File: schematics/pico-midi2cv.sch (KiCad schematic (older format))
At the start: 30 parts, among them J1 Jack-DC, U1 LM7805_TO220, U2 LM358, U3 MCP4822, U4 6N138

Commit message: Updated schematics
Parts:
- removed J_CV1, J_GATE1: CV Out, symbol Connector:AudioJack2
- removed J_SWD_IO1: UART Programming, symbol Connector:Conn_01x02_Male
- added H1, H2, H3: MountingHole, MountingHole:MountingHole_3mm, symbol Mechanical:MountingHole
- added J_CV1: CV Out, Zimo_Manual_PCB:NSL25_01x02_Vertical, symbol Connector:Conn_01x02_Male
- added J_GATE1: Gate Out, Zimo_Manual_PCB:NSL25_01x02_Vertical, symbol Connector:Conn_01x02_Male
- added J_SWD_IO1: UART Programming, Zimo_Manual_PCB:PinOut_01x04, symbol Connector:Conn_01x04_Male
- C1: footprint (none) -> Zimo_Manual_PCB:CP_Radial_D5.0mm_P2.50mm
- C2, C3, C4, C5, C6: footprint (none) -> Zimo_Manual_PCB:C_Disc_D5.0mm_W2.5mm_P2.50mm
- D1: footprint (none) -> Zimo_Manual_PCB:D_Axial
- D_GATE_LED1: footprint (none) -> Zimo_Manual_PCB:NSL25_01x02_Vertical
- J1: value Jack-DC -> Jack-DC (12-32V); footprint (none) -> Zimo_Manual_PCB:NSL25_01x02_Vertical
- J_MIDI_IN1: footprint (none) -> Zimo_Manual_PCB:PinOut_01x05
- Q_GATE_LED1: footprint Package_TO_SOT_THT:TO-92_Inline -> Zimo_Manual_PCB:TO-92_Inline_Wide
- R1, R11, R2, R3, R4, R5, R6, R7, R8, R9: footprint (none) -> Zimo_Manual_PCB:R_Axial_Vertical
- R10: value 220 -> 470; footprint (none) -> Zimo_Manual_PCB:R_Axial_Vertical
- U2, U3, U4: footprint (none) -> Zimo_Manual_PCB:DIP-8_W7.62mm
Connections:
- net +5V: now also J_SWD_IO1.3 (Pin_3)
- net GND: now also J_CV1.2 (Pin_2), J_GATE1.2 (Pin_2), J_SWD_IO1.4 (Pin_4)
- net UART_RX: now also J_SWD_IO1.2 (Pin_2)
- net UART_TX: now also J_SWD_IO1.1 (Pin_1)
- net at R3.1: now also J_CV1.1 (Pin_1)
- net at R8.1: now also J_GATE1.1 (Pin_1)
- no-connect marks 7 -> 31

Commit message: Updated schematics
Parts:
- added D2: 1N4001, Zimo_Manual_PCB:D_Axial, symbol Device:D
- R5: value 22k -> 100k
- R6: value 33k -> 51k
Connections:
- net +12V: now also D2.2 (A); no longer C1.1, C2.1, U1.1 (VI)
- net at C5.1, R3.2, U2.1: no longer R2.1
- net at J_CV1.1 (Pin_1), R3.1: now also R2.1
- new net: C1.1, C2.1, D2.1 (K), U1.1 (VI)
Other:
- note added: "Calibration\n————————\nThe max output of the DAC is 4095mV. At this\npoint the CV output should be 10000mV (10V)\nto cover the 10 octave range. This is an ampli-\nfication of A = 10000 / 4095 = 2.442. This op-amp\nconfiguration provides a fairly close amplification\nto this depending on the accuracy of R1, R2 and R3.\n\nTo further refine the output use the firmware\ncalibration."
- moved on the sheet: C1, C5, C6, D_GATE_LED1, J1, J_GATE1, Q_GATE_LED1, R10, R3, R5, R6, R7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

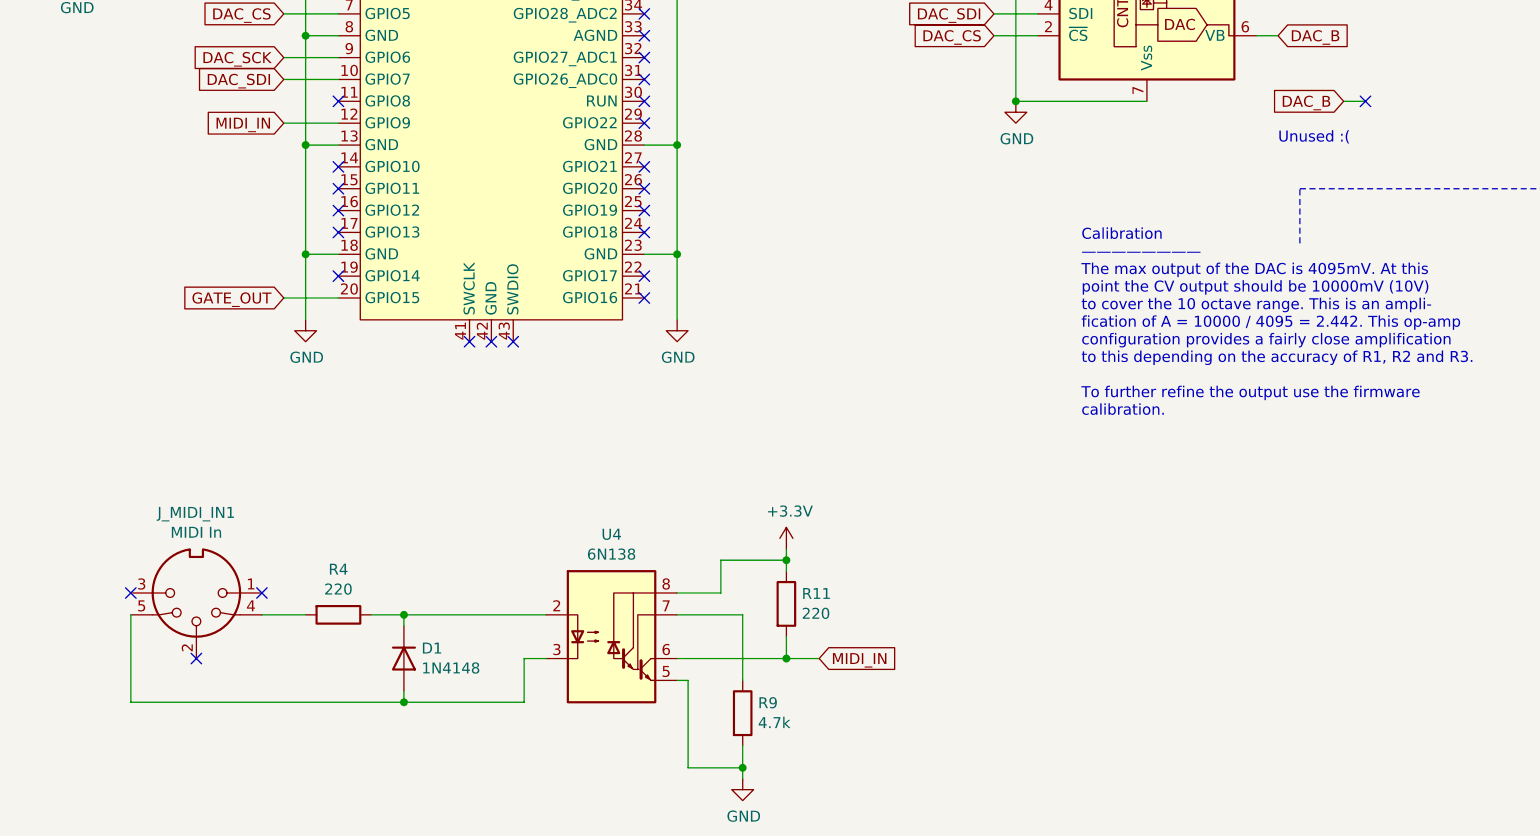
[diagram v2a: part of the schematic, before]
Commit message: Added MIDI channel DIP switch
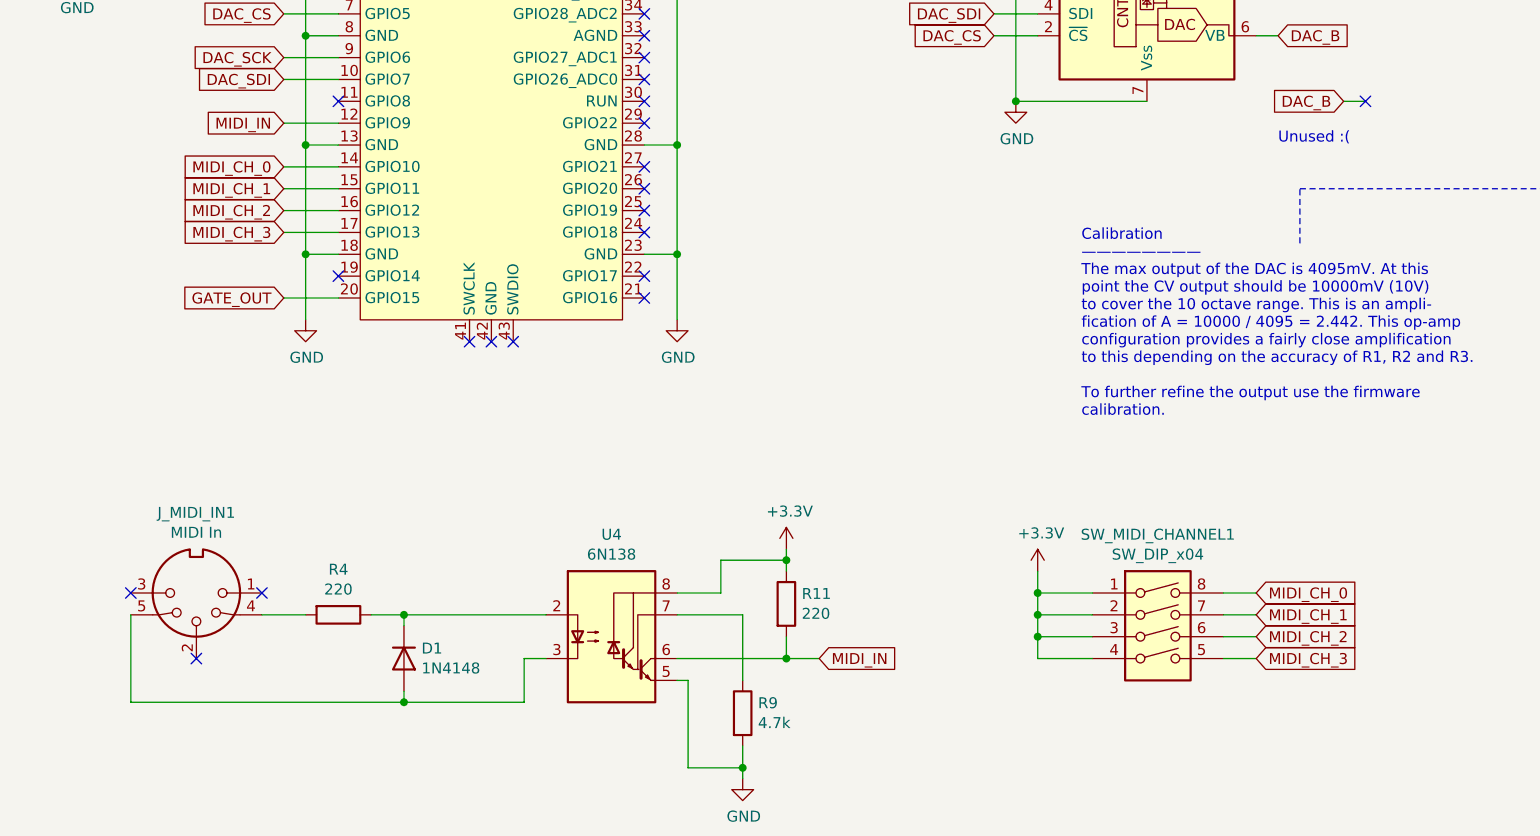
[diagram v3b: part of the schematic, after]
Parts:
- added SW_MIDI_CHANNEL1: SW_DIP_x04, Button_Switch_THT:SW_DIP_SPSTx04_Slide_6.7x11.72mm_W7.62mm_P2.54mm_LowProfile, symbol Switch:SW_DIP_x04
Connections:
- net +3V3: now also SW_MIDI_CHANNEL1.1, SW_MIDI_CHANNEL1.2, SW_MIDI_CHANNEL1.3, SW_MIDI_CHANNEL1.4
- net MIDI_CH_0: now reaches U_PICO1.14 (GPIO10)
- net MIDI_CH_0: now also SW_MIDI_CHANNEL1.8
- net MIDI_CH_1: now reaches U_PICO1.15 (GPIO11)
- net MIDI_CH_1: now also SW_MIDI_CHANNEL1.7
- net MIDI_CH_2: now reaches U_PICO1.16 (GPIO12)
- net MIDI_CH_2: now also SW_MIDI_CHANNEL1.6
- net MIDI_CH_3: now reaches U_PICO1.17 (GPIO13)
- net MIDI_CH_3: now also SW_MIDI_CHANNEL1.5
- no-connect marks 31 -> 27
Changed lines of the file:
@@
 NoConn ~ 2200 1850
 NoConn ~ 2200 2350
-NoConn ~ 2200 2650
-NoConn ~ 2200 2750
-NoConn ~ 2200 2850
-NoConn ~ 2200 2950
 NoConn ~ 2200 3150
 NoConn ~ 3600 1350
@@
 	9300 4100 9300 3750
 Connection ~ 9300 3750
+$Comp
+L Switch:SW_DIP_x04 SW_MIDI_CHANNEL1
+U 1 1 62C690BA
+P 5950 4800
+F 0 "SW_MIDI_CHANNEL1" H 5950 5267 50  0000 C CNN
+F 1 "SW_DIP_x04" H 5950 5176 50  0000 C CNN
+F 2 "Button_Switch_THT:SW_DIP_SPSTx04_Slide_6.7x11.72mm_W7.62mm_P2.54mm_LowProfile" H 5950 4800 50  0001 C CNN
+F 3 "~" H 5950 4800 50  0001 C CNN
+	1    5950 4800
+	1    0    0    -1
+$EndComp
+$Comp
+L power:+3.3V #PWR0102
+U 1 1 62C6CDCC
+P 5400 4500
+F 0 "#PWR0102" H 5400 4350 50  0001 C CNN
+F 1 "+3.3V" H 5415 4673 50  0000 C CNN
+F 2 "" H 5400 4500 50  0001 C CNN
+F 3 "" H 5400 4500 50  0001 C CNN
+	1    5400 4500
+	1    0    0    -1
+$EndComp
+Wire Wire Line
+	5400 4500 5400 4600
+Wire Wire Line
+	5400 4900 5650 4900
+Wire Wire Line
+	5650 4800 5400 4800
+Connection ~ 5400 4800
+Wire Wire Line
+	5400 4800 5400 4900
+Wire Wire Line
+	5650 4700 5400 4700
+Connection ~ 5400 4700
+Wire Wire Line
+	5400 4700 5400 4800
+Wire Wire Line
+	5650 4600 5400 4600
+Connection ~ 5400 4600
+Wire Wire Line
+	5400 4600 5400 4700
+Text GLabel 6400 4600 2    50   Input ~ 0
+MIDI_CH_0
+Wire Wire Line
+	6400 4600 6250 4600
+Text GLabel 6400 4700 2    50   Input ~ 0
+MIDI_CH_1
+Text GLabel 6400 4800 2    50   Input ~ 0
+MIDI_CH_2
+Text GLabel 6400 4900 2    50   Input ~ 0
+MIDI_CH_3
+Wire Wire Line
+	6400 4700 6250 4700
+Wire Wire Line
+	6400 4800 6250 4800
+Wire Wire Line
+	6400 4900 6250 4900
+Text GLabel 1950 2650 0    50   Input ~ 0
+MIDI_CH_0
+Wire Wire Line
+	1950 2650 2200 2650
+Text GLabel 1950 2750 0    50   Input ~ 0
+MIDI_CH_1
+Text GLabel 1950 2850 0    50   Input ~ 0
+MIDI_CH_2
+Text GLabel 1950 2950 0    50   Input ~ 0
+MIDI_CH_3
+Wire Wire Line
+	1950 2750 2200 2750
+Wire Wire Line
+	1950 2850 2200 2850
+Wire Wire Line
+	1950 2950 2200 2950
 $EndSCHEMATC

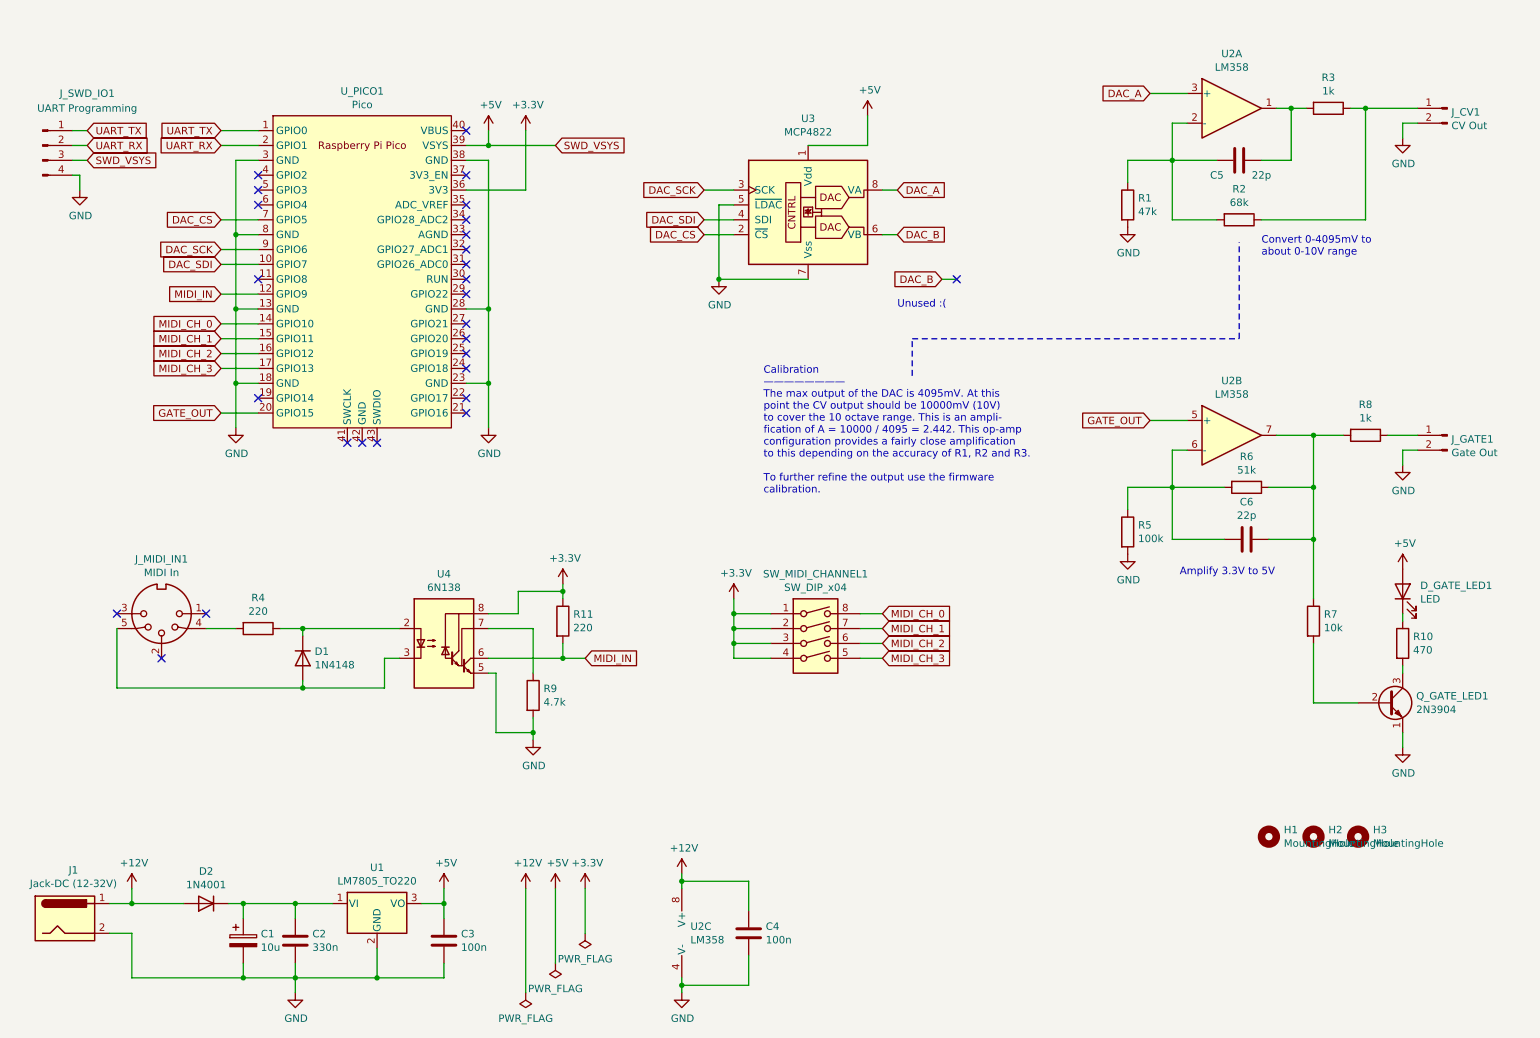
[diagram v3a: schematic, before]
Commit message: Added top 20 pin outs to PCB and further updates
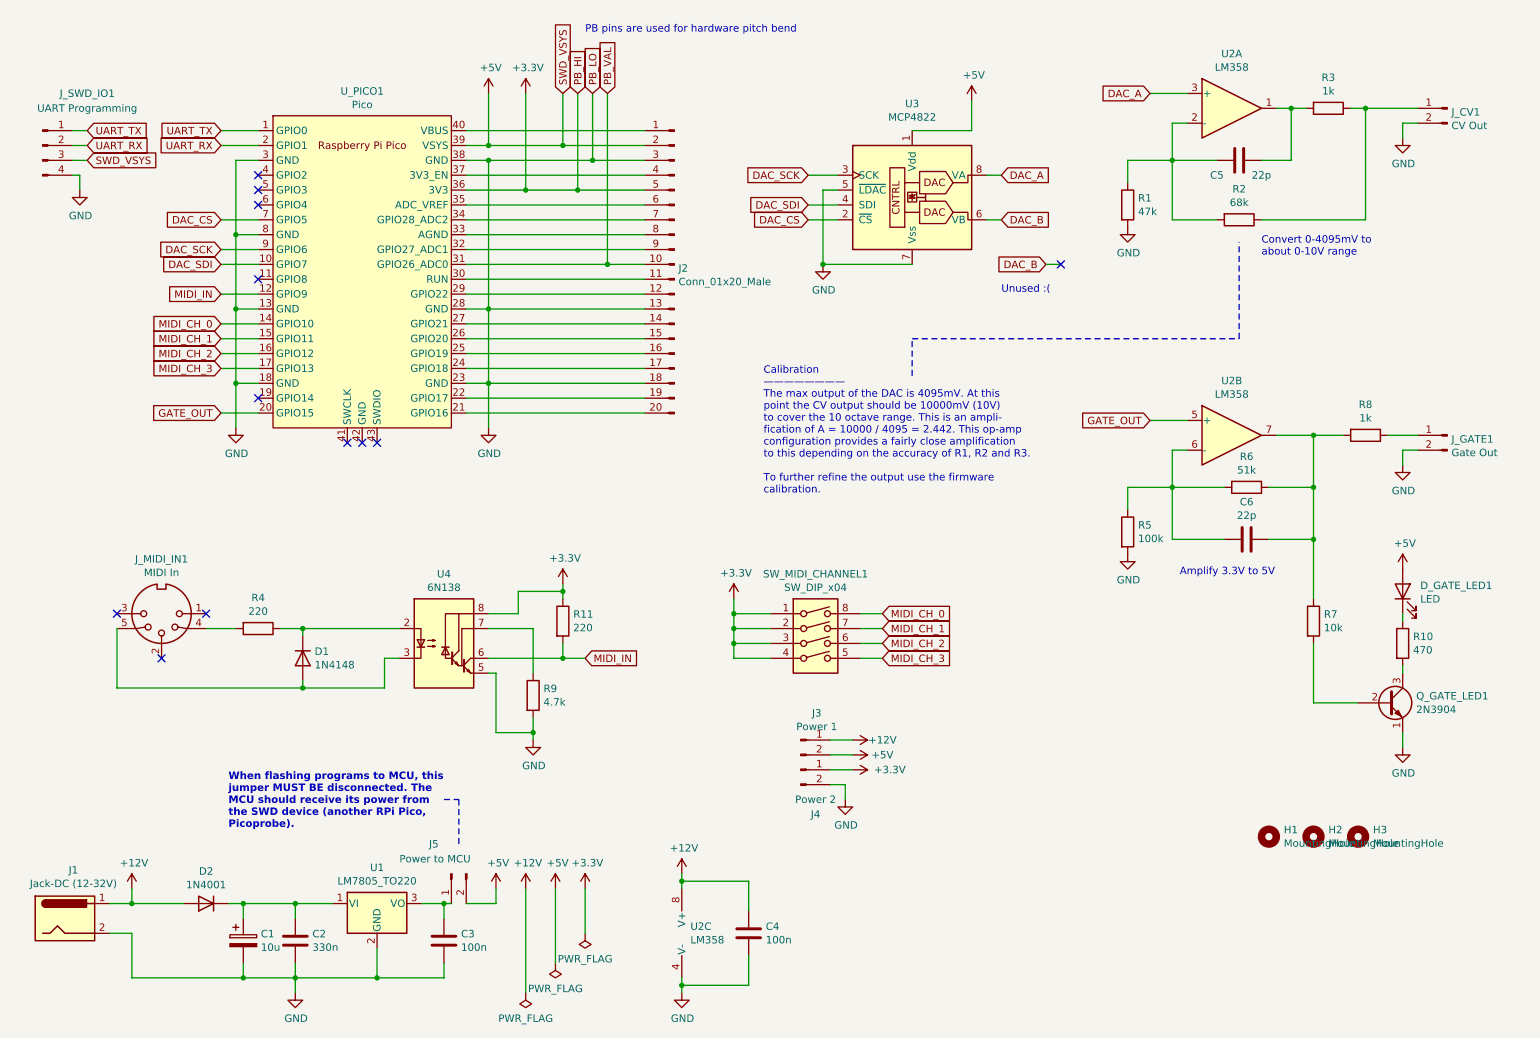
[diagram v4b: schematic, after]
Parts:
- added J2: Conn_01x20_Male, Zimo_Manual_PCB:PinOut_01x20, symbol Connector:Conn_01x20_Male
- added J3: Power 1, Zimo_Manual_PCB:NSL25_01x02_Vertical, symbol Connector:Conn_01x02_Male
- added J4: Power 2, Zimo_Manual_PCB:NSL25_01x02_Vertical, symbol Connector:Conn_01x02_Male
- added J5: Power to MCU, Zimo_Manual_PCB:PinOut_01x02, symbol Connector:Conn_01x02_Male
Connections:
- net +12V: now also J3.1 (Pin_1)
- net +3V3: now also J2.5 (Pin_5), J4.1 (Pin_1)
- net +5V: now also J2.2 (Pin_2), J3.2 (Pin_2), J5.2 (Pin_2); no longer C3.1, U1.3 (VO)
- net GND: now also J2.13 (Pin_13), J2.18 (Pin_18), J2.3 (Pin_3), J4.2 (Pin_2)
- net at U_PICO1.21 (GPIO16): now also J2.20 (Pin_20)
- net at U_PICO1.22 (GPIO17): now also J2.19 (Pin_19)
- net at U_PICO1.24 (GPIO18): now also J2.17 (Pin_17)
- net at U_PICO1.25 (GPIO19): now also J2.16 (Pin_16)
- net at U_PICO1.26 (GPIO20): now also J2.15 (Pin_15)
- net at U_PICO1.27 (GPIO21): now also J2.14 (Pin_14)
- net at U_PICO1.29 (GPIO22): now also J2.12 (Pin_12)
- net at U_PICO1.30 (RUN): now also J2.11 (Pin_11)
- net PB_VAL: now reaches U_PICO1.31 (GPIO26_ADC0)
- net PB_VAL: now also J2.10 (Pin_10)
- net at U_PICO1.32 (GPIO27_ADC1): now also J2.9 (Pin_9)
- net at U_PICO1.33 (AGND): now also J2.8 (Pin_8)
- net at U_PICO1.34 (GPIO28_ADC2): now also J2.7 (Pin_7)
- net at U_PICO1.35 (ADC_VREF): now also J2.6 (Pin_6)
- net at U_PICO1.37 (3V3_EN): now also J2.4 (Pin_4)
- net at U_PICO1.40 (VBUS): now also J2.1 (Pin_1)
- new net: C3.1, J5.1 (Pin_1), U1.3 (VO)
- no-connect marks 27 -> 12
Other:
- note added: "PB pins are used for hardware pitch bend"
- note added: "When flashing programs to MCU, this \njumper MUST BE disconnected. The \nMCU should receive its power from \nthe SWD device (another RPi Pico, \nPicoprobe)."
- moved on the sheet: U3

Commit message: Bugfixes
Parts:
- added J6: MIDI Keyboard Power, Zimo_Manual_PCB:NSL25_01x02_Vertical, symbol Connector:Conn_01x02_Male
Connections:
- net +12V: now also J6.1 (Pin_1)
- net GND: now also J6.2 (Pin_2)
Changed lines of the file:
@@
 Wire Notes Line
 	3550 5850 3550 6150
+$Comp
+L power:+12V #PWR0107
+U 1 1 62F15806
+P 7400 5450
+F 0 "#PWR0107" H 7400 5300 50  0001 C CNN
+F 1 "+12V" V 7400 5650 50  0000 C CNN
+F 2 "" H 7400 5450 50  0001 C CNN
+F 3 "" H 7400 5450 50  0001 C CNN
+	1    7400 5450
+	0    1    1    0
+$EndComp
+Wire Wire Line
+	7400 5450 7200 5450
+$Comp
+L power:GND #PWR0108
+U 1 1 62F20C37
+P 7300 5650
+F 0 "#PWR0108" H 7300 5400 50  0001 C CNN
+F 1 "GND" H 7305 5477 50  0000 C CNN
+F 2 "" H 7300 5650 50  0001 C CNN
+F 3 "" H 7300 5650 50  0001 C CNN
+	1    7300 5650
+	1    0    0    -1
+$EndComp
+Wire Wire Line
+	7300 5650 7300 5550
+Wire Wire Line
+	7300 5550 7200 5550
+$Comp
+L Connector:Conn_01x02_Male J6
+U 1 1 62F2C541
+P 7000 5450
+F 0 "J6" H 7108 5631 50  0000 C CNN
+F 1 "MIDI Keyboard Power" H 7108 5540 50  0000 C CNN
+F 2 "Zimo_Manual_PCB:NSL25_01x02_Vertical" H 7000 5450 50  0001 C CNN
+F 3 "~" H 7000 5450 50  0001 C CNN
+	1    7000 5450
+	1    0    0    -1
+$EndComp
 $EndSCHEMATC
